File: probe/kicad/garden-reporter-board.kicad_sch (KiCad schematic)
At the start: 26 parts, among them J1 70543-0106, J2 Conn_01x02, J3 70543-0002, J4 70543-0002, J5 70543-0002, Q1 TN0702N3-G, U1 MCP1700-3302E_TO92, U2 MCP1700-3302E_TO92, U3 MCP1700-1202E_TO92

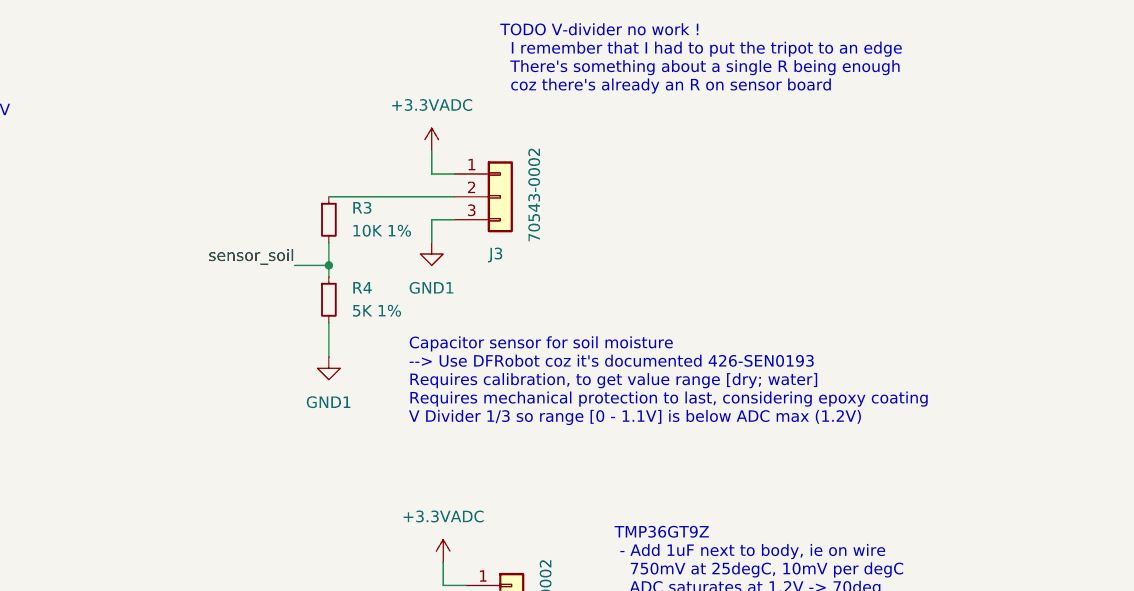
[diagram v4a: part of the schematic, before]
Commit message: Fix voltage output range of soil moist sensor, 1.2V to light sensor
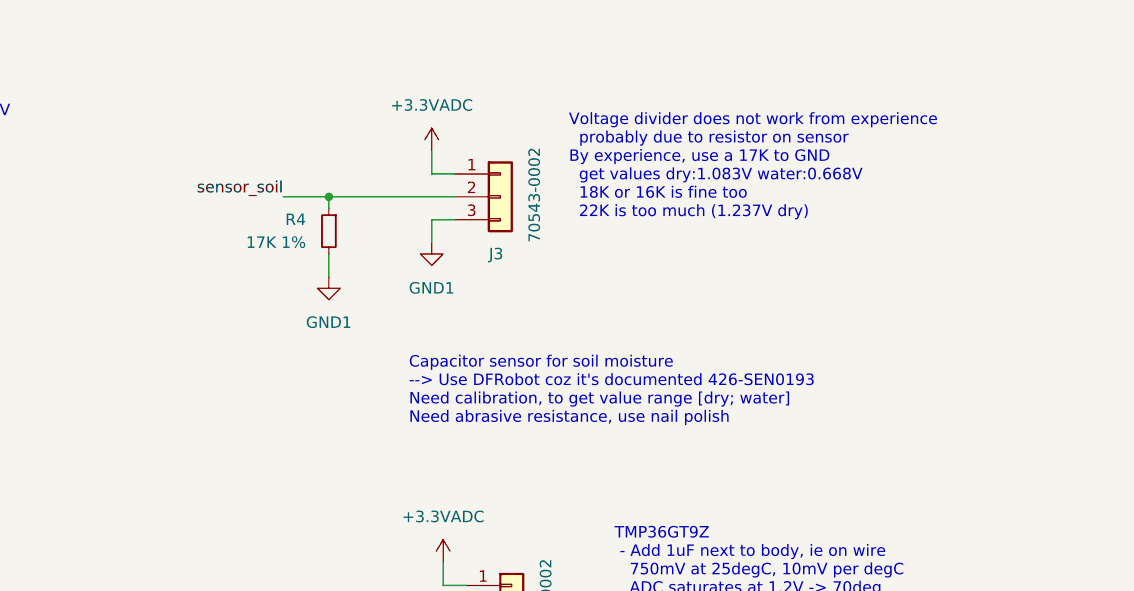
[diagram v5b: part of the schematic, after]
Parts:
- removed R3: 10K 1%, Resistor_THT:R_Axial_DIN0207_L6.3mm_D2.5mm_P7.62mm_Horizontal, symbol Device:R_Small
- R4: value 5K 1% -> 17K 1%
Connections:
- net sensor_soil: now also J3.2 (Pin_2)
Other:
- note added: "Capacitor sensor for soil moisture --> Use DFRobot coz it's documented 426-SEN0193 Need calibration, to get value range [dry; water] Need abrasive resistance, use nail polish"
- note added: "Voltage divider does not work from experience probably due to resistor on sensor By experience, use a 17K to GND get values dry:1.083V water:0.668V 18K or 16K is fine too 22K is too much (1.237V dry)"
- note removed: "Capacitor sensor for soil moisture --> Use DFRobot coz it's documented 426-SEN0193 Requires calibration, to get value range [dry; water] Requires mechanical protection to last, considering epoxy coating V Divider 1/3 so range [0 - 1.1V] is below ADC max (1.2V)"
- note removed: "TODO V-divider no work ! I remember that I had to put the tripot to an edge There's something about a single R being enough coz there's already an R on sensor board"
- moved on the sheet: R4
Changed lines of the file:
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@@
   (junction (at 17.78 21.59) (diameter 0) (color 0 0 0 0)
   )
-  (junction (at 209.55 39.37) (diameter 0) (color 0 0 0 0)
+  (junction (at 209.55 31.75) (diameter 0) (color 0 0 0 0)
   )
   (junction (at 222.25 132.08) (diameter 0) (color 0 0 0 0)
@@
     (stroke (width 0) (type default) (color 0 0 0 0))
   )
-  (wire (pts (xy 209.55 45.72) (xy 209.55 49.53))
+  (wire (pts (xy 209.55 38.1) (xy 209.55 40.64))
     (stroke (width 0) (type default) (color 0 0 0 0))
   )
@@
     (stroke (width 0) (type default) (color 0 0 0 0))
   )
-  (wire (pts (xy 209.55 36.83) (xy 209.55 39.37))
-    (stroke (width 0) (type default) (color 0 0 0 0))
-  )
   (wire (pts (xy 17.78 21.59) (xy 27.94 21.59))
     (stroke (width 0) (type default) (color 0 0 0 0))
@@
     (stroke (width 0) (type default) (color 0 0 0 0))
   )
-  (wire (pts (xy 209.55 39.37) (xy 209.55 40.64))
+  (wire (pts (xy 209.55 31.75) (xy 209.55 33.02))
     (stroke (width 0) (type default) (color 0 0 0 0))
   )
@@
     (stroke (width 0) (type default) (color 0 0 0 0))
   )
-  (wire (pts (xy 205.74 39.37) (xy 209.55 39.37))
+  (wire (pts (xy 204.47 31.75) (xy 209.55 31.75))
     (stroke (width 0) (type default) (color 0 0 0 0))
   )
@@
     (effects (font (size 1.27 1.27)) (justify left bottom))
   )
-  (text "TODO V-divider no work !\n  I remember that I had to put the tripot to an edge\n  There's something about a single R being enough \n  coz there's already an R on sensor board"
-    (at 228.6 20.32 0)
+  (text "Voltage divider does not work from experience\n  probably due to resistor on sensor\nBy experience, use a 17K to GND\n  get values dry:1.083V water:0.668V\n  18K or 16K is fine too\n  22K is too much (1.237V dry)"
+    (at 236.22 34.29 0)
     (effects (font (size 1.27 1.27)) (justify left bottom))
   )
@@
     (effects (font (size 1.27 1.27)) (justify left bottom))
   )
-  (text "Capacitor sensor for soil moisture\n--> Use DFRobot coz it's documented 426-SEN0193\nRequires calibration, to get value range [dry; water]\nRequires mechanical protection to last, considering epoxy coating\nV Divider 1/3 so range [0 - 1.1V] is below ADC max (1.2V)"
+  (text "Capacitor sensor for soil moisture\n--> Use DFRobot coz it's documented 426-SEN0193\nNeed calibration, to get value range [dry; water]\nNeed abrasive resistance, use nail polish"
     (at 218.44 57.15 0)
     (effects (font (size 1.27 1.27)) (justify left bottom))
@@
     (effects (font (size 1.27 1.27)) (justify left bottom))
   )
-  (label "sensor_soil" (at 205.74 39.37 180)
+  (label "sensor_soil" (at 204.47 31.75 180)
     (effects (font (size 1.27 1.27)) (justify right bottom))
   )
@@
     (pin "1")
   )
-  (symbol (lib_id "Device:R_Small") (at 209.55 43.18 0) (unit 1)
+  (symbol (lib_id "Device:R_Small") (at 209.55 35.56 0) (mirror y) (unit 1)
     (in_bom yes) (on_board yes)
-    (property "Reference" "R4" (id 0) (at 212.09 41.9099 0)
-      (effects (font (size 1.27 1.27)) (justify left))
-    )
-    (property "Value" "5K 1%" (id 1) (at 212.09 44.4499 0)
-      (effects (font (size 1.27 1.27)) (justify left))
-    )
-    (property "Footprint" "Resistor_THT:R_Axial_DIN0207_L6.3mm_D2.5mm_P7.62mm_Horizontal" (id 2) (at 209.55 43.18 0)
-      (effects (font (size 1.27 1.27)) hide)
-    )
-    (property "Datasheet" "~" (id 3) (at 209.55 43.18 0)
+    (property "Reference" "R4" (id 0) (at 207.01 34.2899 0)
+      (effects (font (size 1.27 1.27)) (justify left))
+    )
+    (property "Value" "17K 1%" (id 1) (at 207.01 36.8299 0)
+      (effects (font (size 1.27 1.27)) (justify left))
+    )
+    (property "Footprint" "Resistor_THT:R_Axial_DIN0207_L6.3mm_D2.5mm_P7.62mm_Horizontal" (id 2) (at 209.55 35.56 0)
+      (effects (font (size 1.27 1.27)) hide)
+    )
+    (property "Datasheet" "~" (id 3) (at 209.55 35.56 0)
       (effects (font (size 1.27 1.27)) hide)
     )
@@
     (pin "1")
   )
-  (symbol (lib_id "power:GND1") (at 209.55 49.53 0) (unit 1)
-    (in_bom yes) (on_board yes) (fields_autoplaced)
-    (property "Reference" "#PWR019" (id 0) (at 209.55 55.88 0)
-      (effects (font (size 1.27 1.27)) hide)
-    )
-    (property "Value" "GND1" (id 1) (at 209.55 54.61 0))
-    (property "Footprint" "" (id 2) (at 209.55 49.53 0)
-      (effects (font (size 1.27 1.27)) hide)
-    )
-    (property "Datasheet" "" (id 3) (at 209.55 49.53 0)
+  (symbol (lib_id "power:GND1") (at 209.55 40.64 0) (unit 1)
+    (in_bom yes) (on_board yes) (fields_autoplaced)
+    (property "Reference" "#PWR019" (id 0) (at 209.55 46.99 0)
+      (effects (font (size 1.27 1.27)) hide)
+    )
+    (property "Value" "GND1" (id 1) (at 209.55 45.72 0))
+    (property "Footprint" "" (id 2) (at 209.55 40.64 0)
+      (effects (font (size 1.27 1.27)) hide)
+    )
+    (property "Datasheet" "" (id 3) (at 209.55 40.64 0)
       (effects (font (size 1.27 1.27)) hide)
     )
@@
     (pin "1")
   )
-  (symbol (lib_id "Device:R_Small") (at 209.55 34.29 0) (unit 1)
-    (in_bom yes) (on_board yes) (fields_autoplaced)
-    (property "Reference" "R3" (id 0) (at 212.09 33.0199 0)
-      (effects (font (size 1.27 1.27)) (justify left))
-    )
-    (property "Value" "10K 1%" (id 1) (at 212.09 35.5599 0)
-      (effects (font (size 1.27 1.27)) (justify left))
-    )
-    (property "Footprint" "Resistor_THT:R_Axial_DIN0207_L6.3mm_D2.5mm_P7.62mm_Horizontal" (id 2) (at 209.55 34.29 0)
-      (effects (font (size 1.27 1.27)) hide)
-    )
-    (property "Datasheet" "~" (id 3) (at 209.55 34.29 0)
-      (effects (font (size 1.27 1.27)) hide)
-    )
-    (pin "1")
-    (pin "2")
-  )
   (symbol (lib_id "power:-BATT") (at 26.67 46.99 180) (unit 1)
     (in_bom yes) (on_board yes) (fields_autoplaced)
@@
       (reference "R2") (unit 1) (value "2K 1%") (footprint "Resistor_THT:R_Axial_DIN0207_L6.3mm_D2.5mm_P7.62mm_Horizontal")
     )
-    (path "/e1d022a1-6d3e-4f8f-b7ca-283de6842848"
-      (reference "R3") (unit 1) (value "10K 1%") (footprint "Resistor_THT:R_Axial_DIN0207_L6.3mm_D2.5mm_P7.62mm_Horizontal")
-    )
     (path "/118653f1-d23e-4a41-b514-16d86c5ae7fd"
-      (reference "R4") (unit 1) (value "5K 1%") (footprint "Resistor_THT:R_Axial_DIN0207_L6.3mm_D2.5mm_P7.62mm_Horizontal")
+      (reference "R4") (unit 1) (value "17K 1%") (footprint "Resistor_THT:R_Axial_DIN0207_L6.3mm_D2.5mm_P7.62mm_Horizontal")
     )
     (path "/bd38ece9-ca3e-4580-8201-279e6f18db11"

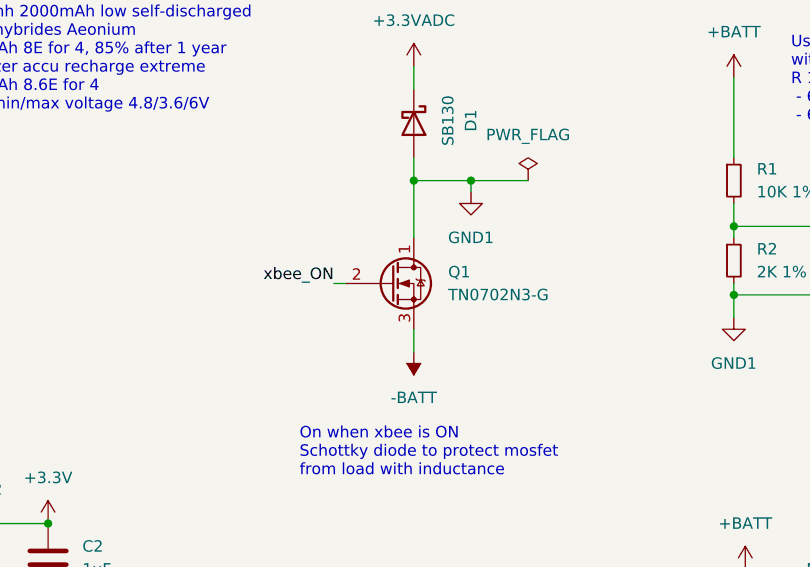
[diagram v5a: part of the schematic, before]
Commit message: Smaller profile. Re-number sensor mosfet pins properly
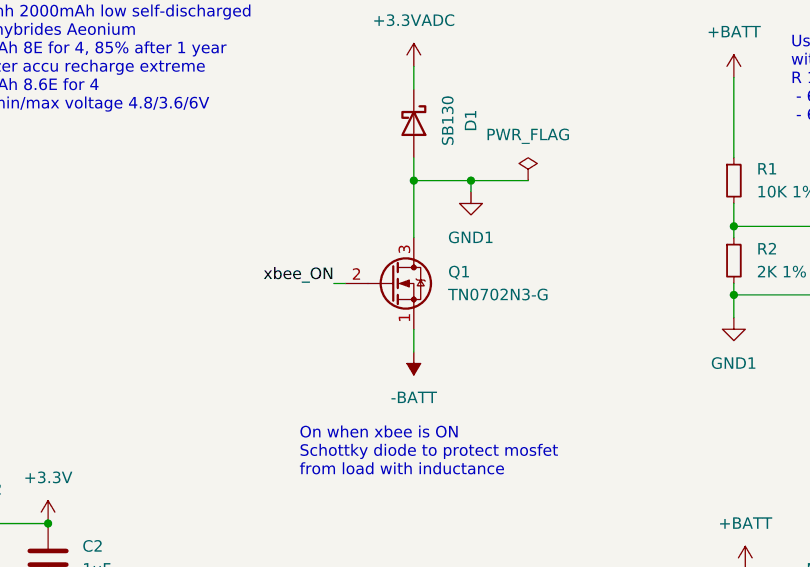
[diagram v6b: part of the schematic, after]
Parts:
- Q1: Spice_Model (none) -> TN0702N3-G; Spice_Netlist_Enabled (none) -> Y; Spice_Primitive (none) -> M
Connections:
- net -BATT: now also Q1.1 (S); no longer Q1.3 (S)
- net GND1: now also Q1.3 (D); no longer Q1.1 (D)
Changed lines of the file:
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@@
       (effects (font (size 1.27 1.27)) hide)
     )
+    (property "Spice_Primitive" "M" (id 4) (at 92.71 46.99 0)
+      (effects (font (size 1.27 1.27)) hide)
+    )
+    (property "Spice_Model" "TN0702N3-G" (id 5) (at 92.71 46.99 0)
+      (effects (font (size 1.27 1.27)) hide)
+    )
+    (property "Spice_Netlist_Enabled" "Y" (id 6) (at 92.71 46.99 0)
+      (effects (font (size 1.27 1.27)) hide)
+    )
+    (pin "3")
+    (pin "2")
     (pin "1")
-    (pin "2")
-    (pin "3")
   )
   (symbol (lib_id "power:+BATT") (at 132.08 78.74 0) (unit 1)

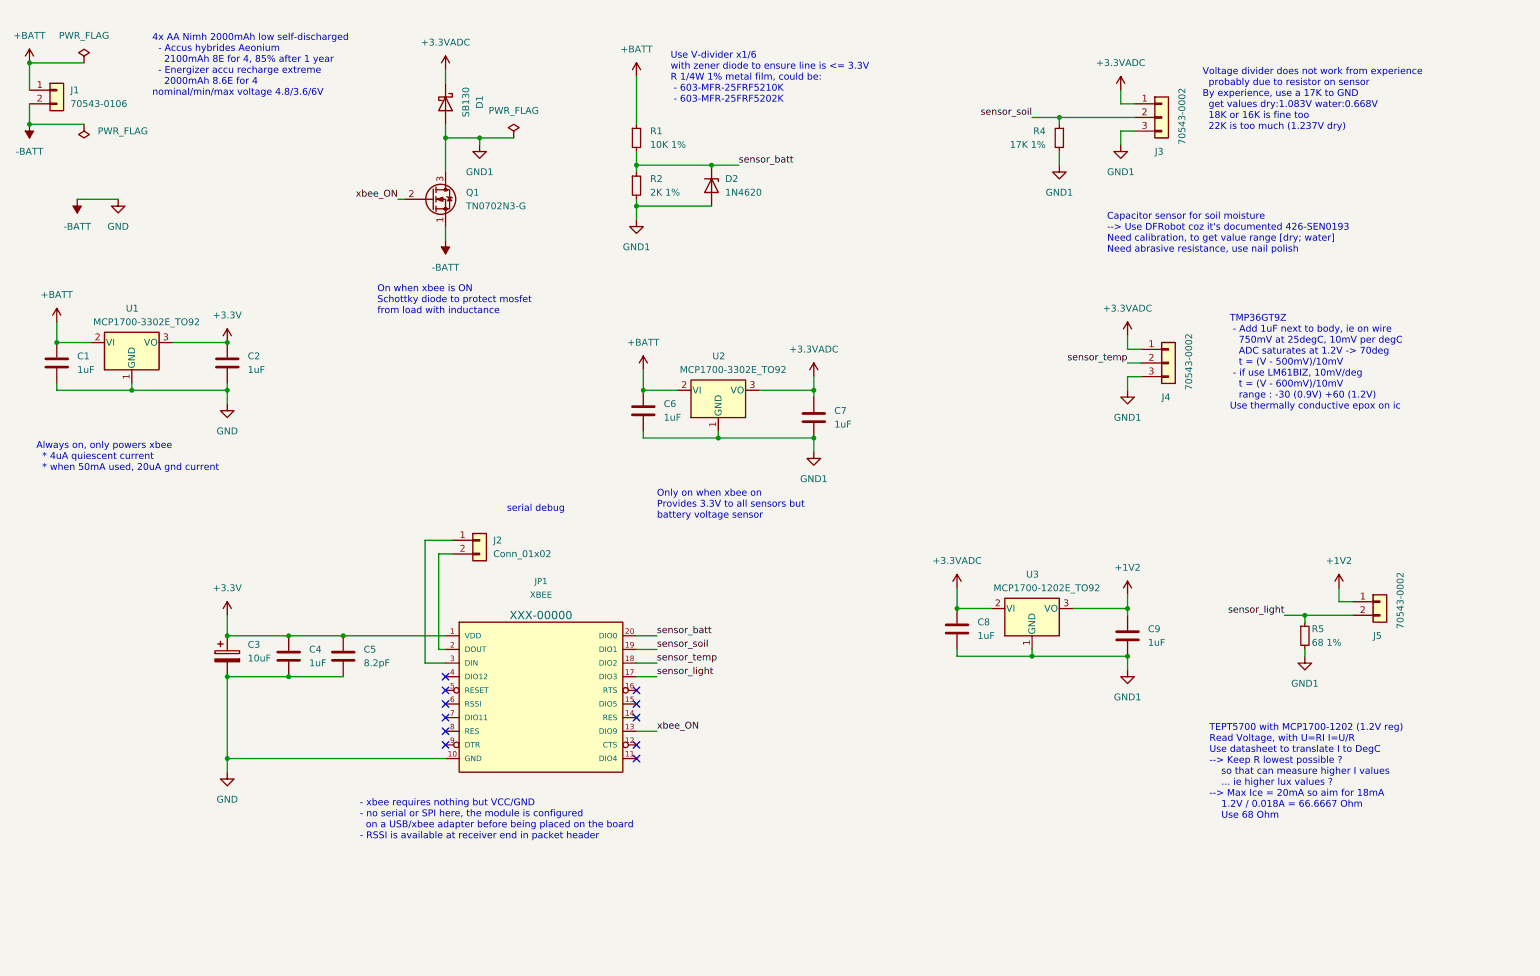
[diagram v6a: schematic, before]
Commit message: Add ceriamic cap for xbee and heavy load sensors, better routing of voltage regulator capacitors, more compact outline
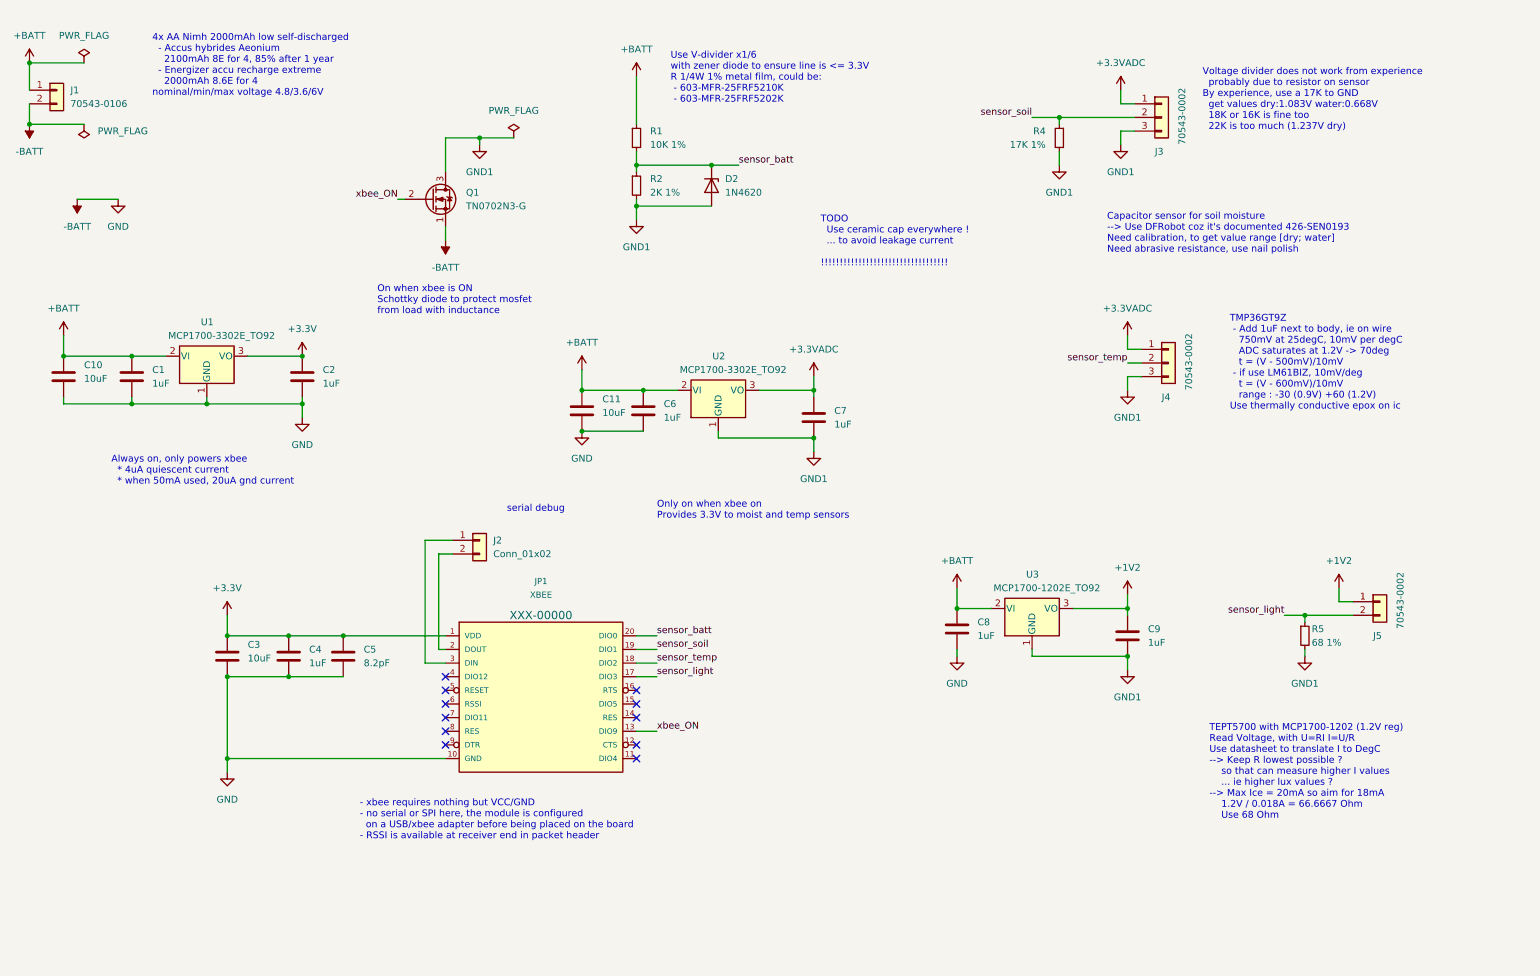
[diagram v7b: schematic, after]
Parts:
- removed C3: 10uF, Capacitor_THT:CP_Radial_D5.0mm_P2.00mm, symbol Device:C_Polarized
- removed D1: SB130, Diode_THT:D_DO-15_P10.16mm_Horizontal, symbol Device:D_Schottky
- added C10, C11, C3: 10uF, Capacitor_THT:C_Disc_D5.0mm_W2.5mm_P2.50mm, symbol Device:C
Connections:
- net +3.3V: now also C3.1
- net +3.3VADC: no longer C8.1, U3.2 (VI)
- net +BATT: now also C8.1, U3.2 (VI), C10.1, C11.1
- net -BATT: now also C6.2, C8.2, C10.2, C11.2, C3.2
- net GND1: no longer C6.2, C8.2
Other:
- note added: "Only on when xbee on Provides 3.3V to moist and temp sensors"
- note added: "TODO Use ceramic cap everywhere ! ... to avoid leakage current !!!!!!!!!!!!!!!!!!!!!!!!!!!!!!!!!!"
- note removed: "Only on when xbee on Provides 3.3V to all sensors but battery voltage sensor"
- moved on the sheet: C1, C2, U1
